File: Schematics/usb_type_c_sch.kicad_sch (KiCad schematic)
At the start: 3 parts, among them J2 USB_C_Receptacle

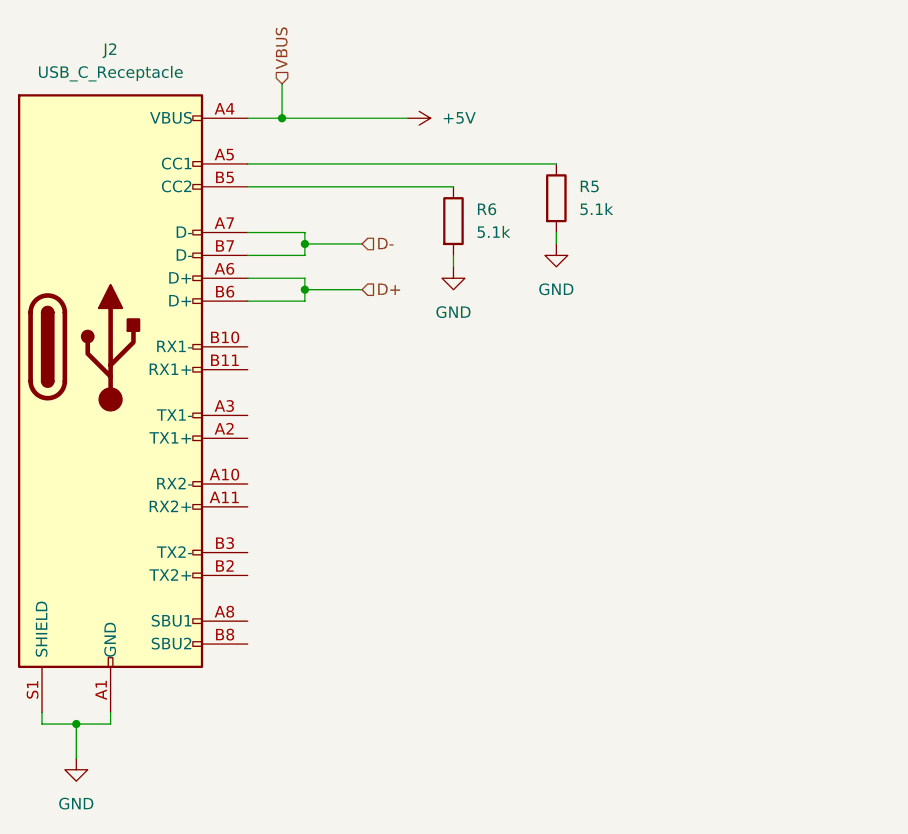
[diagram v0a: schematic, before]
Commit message: assigned footprints ready for pcb design
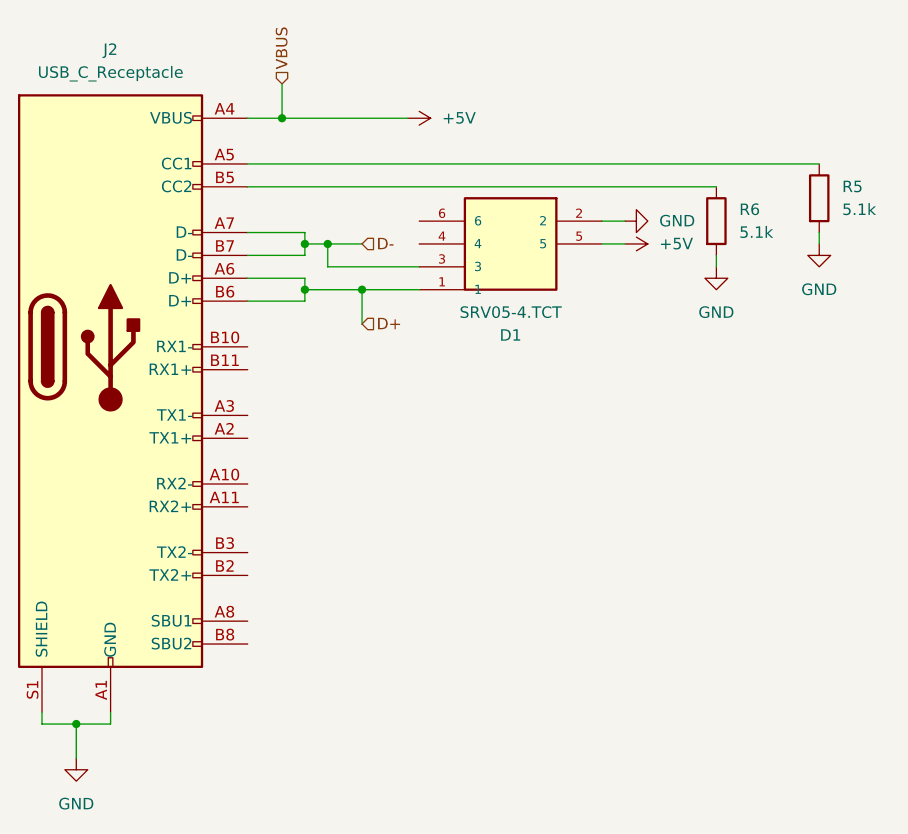
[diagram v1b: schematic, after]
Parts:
- added D1: SRV05-4.TCT, myFootprints:SOT95P280X145-6N, symbol SRV05-4.TCT:SRV05-4.TCT
- J2: footprint (none) -> Connector_USB:USB_C_Receptacle_HRO_TYPE-C-31-M-12
- R5, R6: footprint (none) -> Resistor_SMD:R_0805_2012Metric_Pad1.20x1.40mm_HandSolder
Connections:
- net +5V: now also D1.5
- net D+: now also D1.1
- net D-: now also D1.3
- net GND: now also D1.2
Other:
- moved on the sheet: R5, R6
